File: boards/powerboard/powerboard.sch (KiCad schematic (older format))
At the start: 38 parts, among them J101 RXSM experiment connector, J102 Powerboard <-> Mainboard, J103 Cameraboard, J104 BLDC Motor, J105 BAT, J106 Boost24V_EN, J107 24V_1, J108 24V_1, J109 24V_1, P101 Battery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

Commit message: [powerboard] BLDC motor controller
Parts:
- removed P101: Battery, symbol CONN_01X02
- added J110: BAT, Mounting_Holes:MountingHole_3.2mm_M3_Pad_Via, symbol CONN_01X01
- added J111: GND, Mounting_Holes:MountingHole_3.2mm_M3_Pad_Via, symbol CONN_01X01
- C101, C104, C106, C108: footprint (none) -> Capacitors_SMD:C_0805
- C102: footprint (none) -> Capacitors_SMD:C_1206
- C103, C105, C107: footprint (none) -> Capacitors_SMD:C_0603
- J105: value BAT -> BOOST; footprint (none) -> Mounting_Holes:MountingHole_3.2mm_M3_Pad_Via
- J106: footprint (none) -> Pin_Headers:Pin_Header_Straight_1x01_Pitch2.54mm
- J107: footprint (none) -> Mounting_Holes:MountingHole_3.2mm_M3_Pad_Via
- J108: value 24V_1 -> 24V_2; footprint (none) -> Mounting_Holes:MountingHole_3.2mm_M3_Pad_Via
- J109: value 24V_1 -> 24V_3; footprint (none) -> Mounting_Holes:MountingHole_3.2mm_M3_Pad_Via
- L101: footprint (none) -> Inductors_SMD:L_Fastron_PISR_Handsoldering
- R101, R102, R103, R104, R105, R106, R107, R108, R109, R110, R111, R112: footprint (none) -> Resistors_SMD:R_0603
- U102: footprint (none) -> Housings_SOIC:SOIC-16_3.9x9.9mm_Pitch1.27mm
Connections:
- net BAT_raw: now also J110.1 (P1)
- net GND: now also J111.1 (P1)
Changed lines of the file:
@@
 LIBS:ds26lv32at
 LIBS:drv8312
+LIBS:drv8332
 LIBS:powerboard-cache
 EELAYER 25 0
@@
 $EndComp
 $Comp
-L CONN_01X02 P101
-U 1 1 5886EA99
-P 1150 3050
-F 0 "P101" H 1150 3200 50  0000 C CNN
-F 1 "Battery" V 1250 3050 50  0000 C CNN
-F 2 "" H 1150 3050 50  0000 C CNN
-F 3 "" H 1150 3050 50  0000 C CNN
-	1    1150 3050
-	-1   0    0    1
-$EndComp
-$Comp
 L +5V #PWR109
 U 1 1 5886FF1B
@@
 F 0 "Q104" V 9050 1450 50  0000 R CNN
 F 1 "N-MOS" V 9150 1650 50  0000 R CNN
-F 2 "" H 9350 1350 50  0000 C CNN
+F 2 "" H 9350 1350 50  0001 C CNN
 F 3 "" H 9150 1250 50  0000 C CNN
 	1    9150 1250
@@
 F 0 "U101" H 7850 5450 50  0000 C CNN
 F 1 "LM1117-3.3" H 7750 5950 50  0000 C CNN
-F 2 "" H 7750 5700 50  0000 C CNN
+F 2 "" H 7750 5700 50  0001 C CNN
 F 3 "" H 7750 5700 50  0000 C CNN
 	1    7750 5700
@@
 F 0 "C105" H 7375 6050 50  0000 L CNN
 F 1 "100n" H 7375 5850 50  0000 L CNN
-F 2 "" H 7388 5800 50  0000 C CNN
+F 2 "Capacitors_SMD:C_0603" H 7388 5800 50  0001 C CNN
 F 3 "" H 7350 5950 50  0000 C CNN
 	1    7350 5950
@@
 F 0 "C107" H 8175 6050 50  0000 L CNN
 F 1 "100n" H 8175 5850 50  0000 L CNN
-F 2 "" H 8188 5800 50  0000 C CNN
+F 2 "Capacitors_SMD:C_0603" H 8188 5800 50  0001 C CNN
 F 3 "" H 8150 5950 50  0000 C CNN
 	1    8150 5950
@@
 F 0 "C108" H 8425 6050 50  0000 L CNN
 F 1 "10µ" H 8425 5850 50  0000 L CNN
-F 2 "" H 8438 5800 50  0000 C CNN
+F 2 "Capacitors_SMD:C_0805" H 8438 5800 50  0001 C CNN
 F 3 "" H 8400 5950 50  0000 C CNN
 	1    8400 5950
@@
 F 0 "C104" H 7125 6050 50  0000 L CNN
 F 1 "10µ" H 7125 5850 50  0000 L CNN
-F 2 "" H 7138 5800 50  0000 C CNN
+F 2 "Capacitors_SMD:C_0805" H 7138 5800 50  0001 C CNN
 F 3 "" H 7100 5950 50  0000 C CNN
 	1    7100 5950
@@
 F 0 "L101" H 7200 3000 50  0000 C CNN
 F 1 "10µH" H 7200 2850 50  0000 C CNN
-F 2 "" H 7200 2900 50  0000 C CNN
+F 2 "Inductors_SMD:L_Fastron_PISR_Handsoldering" H 7200 2900 50  0001 C CNN
 F 3 "" H 7200 2900 50  0000 C CNN
 	1    7200 2900
@@
 F 0 "C106" H 7575 3250 50  0000 L CNN
 F 1 "10µ" H 7575 3050 50  0000 L CNN
-F 2 "" H 7588 3000 50  0000 C CNN
+F 2 "Capacitors_SMD:C_0805" H 7588 3000 50  0001 C CNN
 F 3 "" H 7550 3150 50  0000 C CNN
 	1    7550 3150
@@
 F 0 "Q102" H 3000 3700 50  0000 R CNN
 F 1 "N-FET" H 3150 3600 50  0000 R CNN
-F 2 "" H 2900 3750 50  0000 C CNN
+F 2 "" H 2900 3750 50  0001 C CNN
 F 3 "" H 2700 3650 50  0000 C CNN
 	1    2700 3650
@@
 F 0 "R103" V 2480 3900 50  0000 C CNN
 F 1 "10k" V 2400 3900 50  0000 C CNN
-F 2 "" V 2330 3900 50  0000 C CNN
+F 2 "Resistors_SMD:R_0603" V 2330 3900 50  0001 C CNN
 F 3 "" H 2400 3900 50  0000 C CNN
 	1    2400 3900
@@
 F 0 "R102" V 2230 3650 50  0000 C CNN
 F 1 "20k" V 2150 3650 50  0000 C CNN
-F 2 "" V 2080 3650 50  0000 C CNN
+F 2 "Resistors_SMD:R_0603" V 2080 3650 50  0001 C CNN
 F 3 "" H 2150 3650 50  0000 C CNN
 	1    2150 3650
@@
 F 0 "C102" H 2475 1450 50  0000 L CNN
 F 1 "47µ" H 2475 1250 50  0000 L CNN
-F 2 "" H 2488 1200 50  0000 C CNN
+F 2 "Capacitors_SMD:C_1206" H 2488 1200 50  0001 C CNN
 F 3 "" H 2450 1350 50  0000 C CNN
 	1    2450 1350
@@
 F 0 "C103" H 6875 3250 50  0000 L CNN
 F 1 "1µ" H 6875 3050 50  0000 L CNN
-F 2 "" H 6888 3000 50  0000 C CNN
+F 2 "Capacitors_SMD:C_0603" H 6888 3000 50  0001 C CNN
 F 3 "" H 6850 3150 50  0000 C CNN
 	1    6850 3150
@@
 F 0 "Q101" V 2250 3400 50  0000 R CNN
 F 1 "P-FET" V 2050 3450 50  0000 R CNN
-F 2 "" H 2300 3200 50  0000 C CNN
+F 2 "" H 2300 3200 50  0001 C CNN
 F 3 "" H 2100 3100 50  0000 C CNN
 	1    2100 3100
@@
 F 0 "R101" V 1930 3250 50  0000 C CNN
 F 1 "10k" V 1850 3250 50  0000 C CNN
-F 2 "" V 1780 3250 50  0000 C CNN
+F 2 "Resistors_SMD:R_0603" V 1780 3250 50  0001 C CNN
 F 3 "" H 1850 3250 50  0000 C CNN
 	1    1850 3250
@@
 L GND #PWR103
 U 1 1 58CABA0F
-P 1350 3200
-F 0 "#PWR103" H 1350 2950 50  0001 C CNN
-F 1 "GND" H 1350 3050 50  0000 C CNN
-F 2 "" H 1350 3200 50  0000 C CNN
-F 3 "" H 1350 3200 50  0000 C CNN
-	1    1350 3200
+P 1500 3300
+F 0 "#PWR103" H 1500 3050 50  0001 C CNN
+F 1 "GND" H 1500 3150 50  0000 C CNN
+F 2 "" H 1500 3300 50  0000 C CNN
+F 3 "" H 1500 3300 50  0000 C CNN
+	1    1500 3300
 	1    0    0    -1
 $EndComp
@@
 F 0 "R112" V 8930 1200 50  0000 C CNN
 F 1 "100k" V 8850 1200 50  0000 C CNN
-F 2 "" V 8780 1200 50  0001 C CNN
+F 2 "Resistors_SMD:R_0603" V 8780 1200 50  0001 C CNN
 F 3 "" H 8850 1200 50  0001 C CNN
 	1    8850 1200
@@
 F 0 "R110" V 8630 950 50  0000 C CNN
 F 1 "1k" V 8550 950 50  0000 C CNN
-F 2 "" V 8480 950 50  0001 C CNN
+F 2 "Resistors_SMD:R_0603" V 8480 950 50  0001 C CNN
 F 3 "" H 8550 950 50  0001 C CNN
 	1    8550 950
@@
 F 0 "R111" V 10130 5500 50  0000 C CNN
 F 1 "1k" V 10050 5500 50  0000 C CNN
-F 2 "" V 9980 5500 50  0001 C CNN
+F 2 "Resistors_SMD:R_0603" V 9980 5500 50  0001 C CNN
 F 3 "" H 10050 5500 50  0001 C CNN
 	1    10050 5500
@@
 F 0 "C101" H 2425 2350 50  0000 L CNN
 F 1 "10µ" H 2425 2150 50  0000 L CNN
-F 2 "" H 2438 2100 50  0000 C CNN
+F 2 "Capacitors_SMD:C_0805" H 2438 2100 50  0001 C CNN
 F 3 "" H 2400 2250 50  0000 C CNN
 	1    2400 2250
@@
 F 0 "R104" V 2880 5350 50  0000 C CNN
 F 1 "91k" V 2800 5350 50  0000 C CNN
-F 2 "" V 2730 5350 50  0001 C CNN
+F 2 "Resistors_SMD:R_0603" V 2730 5350 50  0001 C CNN
 F 3 "" H 2800 5350 50  0001 C CNN
 	1    2800 5350
@@
 F 0 "R106" V 3080 5350 50  0000 C CNN
 F 1 "15k" V 3000 5350 50  0000 C CNN
-F 2 "" V 2930 5350 50  0001 C CNN
+F 2 "Resistors_SMD:R_0603" V 2930 5350 50  0001 C CNN
 F 3 "" H 3000 5350 50  0001 C CNN
 	1    3000 5350
@@
 F 0 "R107" V 3080 5950 50  0000 C CNN
 F 1 "1k" V 3000 5950 50  0000 C CNN
-F 2 "" V 2930 5950 50  0001 C CNN
+F 2 "Resistors_SMD:R_0603" V 2930 5950 50  0001 C CNN
 F 3 "" H 3000 5950 50  0001 C CNN
 	1    3000 5950
@@
 F 0 "R105" V 2880 5950 50  0000 C CNN
 F 1 "13k" V 2800 5950 50  0000 C CNN
-F 2 "" V 2730 5950 50  0001 C CNN
+F 2 "Resistors_SMD:R_0603" V 2730 5950 50  0001 C CNN
 F 3 "" H 2800 5950 50  0001 C CNN
 	1    2800 5950
@@
 F 0 "R108" V 3280 5350 50  0000 C CNN
 F 1 "15k" V 3200 5350 50  0000 C CNN
-F 2 "" V 3130 5350 50  0001 C CNN
+F 2 "Resistors_SMD:R_0603" V 3130 5350 50  0001 C CNN
 F 3 "" H 3200 5350 50  0001 C CNN
 	1    3200 5350
@@
 F 0 "R109" V 3280 5950 50  0000 C CNN
 F 1 "1k" V 3200 5950 50  0000 C CNN
-F 2 "" V 3130 5950 50  0001 C CNN
+F 2 "Resistors_SMD:R_0603" V 3130 5950 50  0001 C CNN
 F 3 "" H 3200 5950 50  0001 C CNN
 	1    3200 5950
@@
 P 3300 3000
 F 0 "J105" H 3300 3100 50  0000 C CNN
-F 1 "BAT" V 3400 3000 50  0000 C CNN
-F 2 "" H 3300 3000 50  0001 C CNN
+F 1 "BOOST" V 3400 3000 50  0000 C CNN
+F 2 "Mounting_Holes:MountingHole_3.2mm_M3_Pad_Via" H 3300 3000 50  0001 C CNN
 F 3 "" H 3300 3000 50  0001 C CNN
 	1    3300 3000
@@
 F 0 "J106" H 3300 3350 50  0000 C CNN
 F 1 "Boost24V_EN" H 3200 3150 50  0000 C CNN
-F 2 "" H 3300 3250 50  0001 C CNN
+F 2 "Pin_Headers:Pin_Header_Straight_1x01_Pitch2.54mm" H 3300 3250 50  0001 C CNN
 F 3 "" H 3300 3250 50  0001 C CNN
 	1    3300 3250
@@
 F 0 "J107" H 3700 3100 50  0000 C CNN
 F 1 "24V_1" V 3800 3000 50  0000 C CNN
-F 2 "" H 3700 3000 50  0001 C CNN
+F 2 "Mounting_Holes:MountingHole_3.2mm_M3_Pad_Via" H 3700 3000 50  0001 C CNN
 F 3 "" H 3700 3000 50  0001 C CNN
 	1    3700 3000
@@
 P 3700 3250
 F 0 "J108" H 3700 3350 50  0000 C CNN
-F 1 "24V_1" V 3800 3250 50  0000 C CNN
-F 2 "" H 3700 3250 50  0001 C CNN
+F 1 "24V_2" V 3800 3250 50  0000 C CNN
+F 2 "Mounting_Holes:MountingHole_3.2mm_M3_Pad_Via" H 3700 3250 50  0001 C CNN
 F 3 "" H 3700 3250 50  0001 C CNN
 	1    3700 3250
@@
 P 3700 3500
 F 0 "J109" H 3700 3600 50  0000 C CNN
-F 1 "24V_1" V 3800 3500 50  0000 C CNN
-F 2 "" H 3700 3500 50  0001 C CNN
+F 1 "24V_3" V 3800 3500 50  0000 C CNN
+F 2 "Mounting_Holes:MountingHole_3.2mm_M3_Pad_Via" H 3700 3500 50  0001 C CNN
 F 3 "" H 3700 3500 50  0001 C CNN
 	1    3700 3500
@@
 F 0 "U102" H 8600 4300 60  0000 C CNN
 F 1 "DS26LV32AT" H 8600 5400 60  0000 C CNN
-F 2 "" H 8700 4650 60  0001 C CNN
+F 2 "Housings_SOIC:SOIC-16_3.9x9.9mm_Pitch1.27mm" H 8700 4650 60  0001 C CNN
 F 3 "" H 8700 4650 60  0001 C CNN
 	1    8600 4850
@@
 	1550 2150 1050 2150
 Wire Wire Line
-	1350 3100 1350 3200
+	1500 3150 1500 3300
 Wire Wire Line
 	1350 3000 1900 3000
@@
 Wire Wire Line
 	10050 3300 10800 3300
+$Comp
+L CONN_01X01 J110
+U 1 1 5938B3B7
+P 1150 3000
+F 0 "J110" H 1150 2900 50  0000 C CNN
+F 1 "BAT" V 1250 3000 50  0000 C CNN
+F 2 "Mounting_Holes:MountingHole_3.2mm_M3_Pad_Via" H 1150 3000 50  0001 C CNN
+F 3 "" H 1150 3000 50  0001 C CNN
+	1    1150 3000
+	-1   0    0    1
+$EndComp
+$Comp
+L CONN_01X01 J111
+U 1 1 5938BEA1
+P 1150 3150
+F 0 "J111" H 1150 3250 50  0000 C CNN
+F 1 "GND" V 1250 3150 50  0000 C CNN
+F 2 "Mounting_Holes:MountingHole_3.2mm_M3_Pad_Via" H 1150 3150 50  0001 C CNN
+F 3 "" H 1150 3150 50  0001 C CNN
+	1    1150 3150
+	-1   0    0    1
+$EndComp
+Wire Wire Line
+	1500 3150 1350 3150
 $EndSCHEMATC

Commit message: [powerboard] selected all components and assigned all footprints
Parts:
- removed Q102: N-FET, symbol Q_NMOS_GDS
- added Q102: DMN6140L, TO_SOT_Packages_SMD:SOT-23, symbol Q_NMOS_GSD
- FL101: value 10µH 1.5A -> 744272471; footprint (none) -> WE-SLx:WE-SL5
- FL102: value 10µH 1A -> 744272471; footprint (none) -> WE-SLx:WE-SL5
- J101: footprint (none) -> Connectors:DB9MD
- J103: footprint (none) -> Connectors:DB9FD
- J104: footprint (none) -> Connectors:DB15FD
- Q101: value P-FET -> SQM40031EL; footprint (none) -> TO_SOT_Packages_SMD:TO-263-3Lead
- Q104: value N-MOS -> DMN6140L; footprint (none) -> TO_SOT_Packages_SMD:SOT-23
- U101: footprint (none) -> TO_SOT_Packages_SMD:SOT-223-3Lead_TabPin2
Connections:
- net +5V: now also J103.6
- net GND: now also Q102.2 (S)
- net at R102.1, R103.1: now also Q102.1 (G)
- net at Q101.1 (G), R101.2: now also Q102.3 (D)
- no-connect marks 11 -> 10
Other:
- note added: "Common mode chokes:\n2x Würth 744272471\nWE-SL5 SMD 470µH 1.6A"

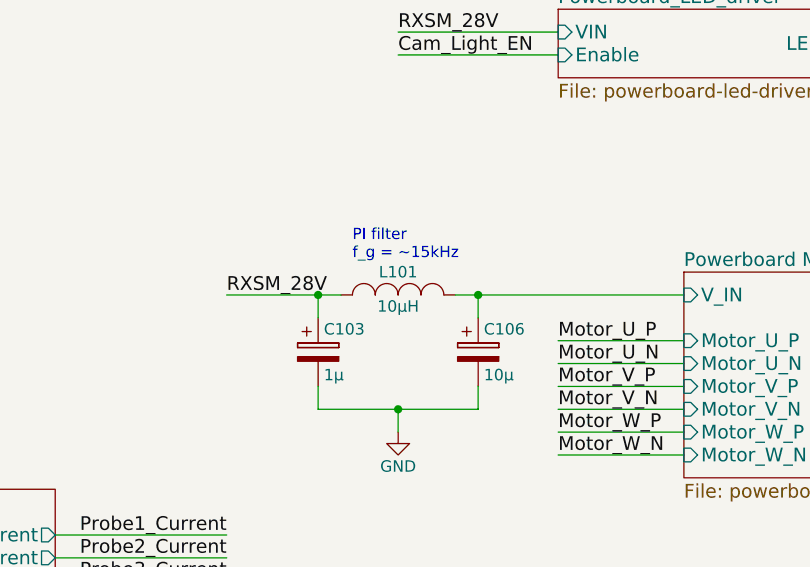
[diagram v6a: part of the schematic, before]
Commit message: [powerboard] select inductors, assign footprints; import netlist in PCB
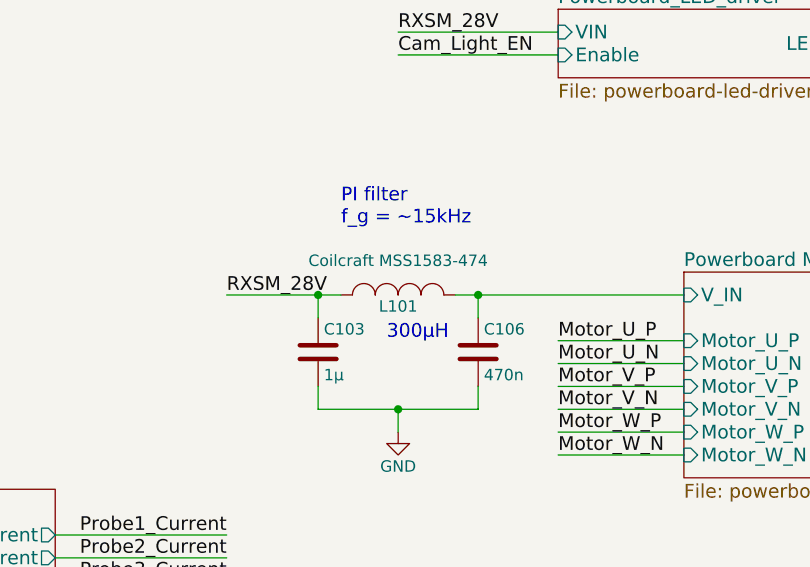
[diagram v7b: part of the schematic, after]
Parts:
- removed C103: 1µ, Capacitors_SMD:C_0603, symbol CP
- removed C106: 10µ, Capacitors_SMD:C_0805, symbol CP
- added C103: 1µ, Capacitors_SMD:C_0805, symbol C
- added C106: 470n, Capacitors_SMD:C_0805, symbol C
- L101: value 10µH -> Coilcraft MSS1583-474; footprint Inductors_SMD:L_Fastron_PISR_Handsoldering -> L_Coilcraft:L_Coilcraft_1583_Handsoldering
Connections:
- net GND: now also C103.2, C106.2
- net Powerboard Motor Controller/V_IN: now also C106.1
- net RXSM_28V: now also C103.1
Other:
- note added: "300µH"
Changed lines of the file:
@@
 U 1 1 588AFDA8
 P 7200 2900
-F 0 "L101" H 7200 3000 50  0000 C CNN
-F 1 "10µH" H 7200 2850 50  0000 C CNN
-F 2 "Inductors_SMD:L_Fastron_PISR_Handsoldering" H 7200 2900 50  0001 C CNN
+F 0 "L101" H 7200 2850 50  0000 C CNN
+F 1 "Coilcraft MSS1583-474" H 7200 3050 50  0000 C CNN
+F 2 "L_Coilcraft:L_Coilcraft_1583_Handsoldering" H 7200 2900 50  0001 C CNN
 F 3 "" H 7200 2900 50  0000 C CNN
 	1    7200 2900
-	1    0    0    -1
-$EndComp
-$Comp
-L CP C106
-U 1 1 588B171D
-P 7550 3150
-F 0 "C106" H 7575 3250 50  0000 L CNN
-F 1 "10µ" H 7575 3050 50  0000 L CNN
-F 2 "Capacitors_SMD:C_0805" H 7588 3000 50  0001 C CNN
-F 3 "" H 7550 3150 50  0000 C CNN
-	1    7550 3150
 	1    0    0    -1
 $EndComp
@@
 	1    0    0    -1
 $EndComp
-Text Notes 7000 2750 0    49   ~ 0
+Text Notes 6950 2600 0    60   ~ 0
 PI filter\nf_g = ~~15kHz
 $Comp
@@
 Text Notes 2450 1000 0    49   ~ 0
 Max. input capacity on \nRXSM 28V: 100µF\n\nDon't assemble input \ncapacitors >1µF in voltage \nregulator sub-schematics!
-$Comp
-L CP C103
-U 1 1 58CAB676
-P 6850 3150
-F 0 "C103" H 6875 3250 50  0000 L CNN
-F 1 "1µ" H 6875 3050 50  0000 L CNN
-F 2 "Capacitors_SMD:C_0603" H 6888 3000 50  0001 C CNN
-F 3 "" H 6850 3150 50  0000 C CNN
-	1    6850 3150
-	1    0    0    -1
-$EndComp
 $Comp
 L CMC FL102
@@
 Text Notes 1250 800  0    60   ~ 0
 Common mode chokes:\n2x Würth 744272471\nWE-SL5 SMD 470µH 1.6A
+$Comp
+L C C106
+U 1 1 5941DCC3
+P 7550 3150
+F 0 "C106" H 7575 3250 50  0000 L CNN
+F 1 "470n" H 7575 3050 50  0000 L CNN
+F 2 "Capacitors_SMD:C_0805" H 7588 3000 50  0001 C CNN
+F 3 "" H 7550 3150 50  0001 C CNN
+	1    7550 3150
+	1    0    0    -1
+$EndComp
+$Comp
+L C C103
+U 1 1 5941E73A
+P 6850 3150
+F 0 "C103" H 6875 3250 50  0000 L CNN
+F 1 "1µ" H 6875 3050 50  0000 L CNN
+F 2 "Capacitors_SMD:C_0805" H 6888 3000 50  0001 C CNN
+F 3 "" H 6850 3150 50  0001 C CNN
+	1    6850 3150
+	1    0    0    -1
+$EndComp
+Text Notes 7150 3100 0    60   ~ 0
+300µH
 $EndSCHEMATC
